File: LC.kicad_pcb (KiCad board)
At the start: 2 copper layers, 60 x 65 mm, 86 parts, among them J1 INPUT+, J10 DISPLAY, J11 ENTER_BUTTON, J12 UP_BUTTON, J2 INPUT-, J3 Barrel_Jack, J4 EXT_CLK, J5 CLKSRC, J6 SIGSRC, J7 EXT_SIG, J8 UNUSED, J9 PROG, Q1 BC817, Q2 BC817, SW1 RESET_BTN, U1 Omron_G2V, U10 74HC590PW,118, U11 74HCS251, U12 AVR32DB28x-xSO, U2 L7805, U3 74AHC1G04, U4 Omron_G2E, U5 74AHC1G14, U6 74AHC1G04, U7 LT1719CS6, U8 74AUC1G74, U9 74AUC2G125, Y1 10MHz

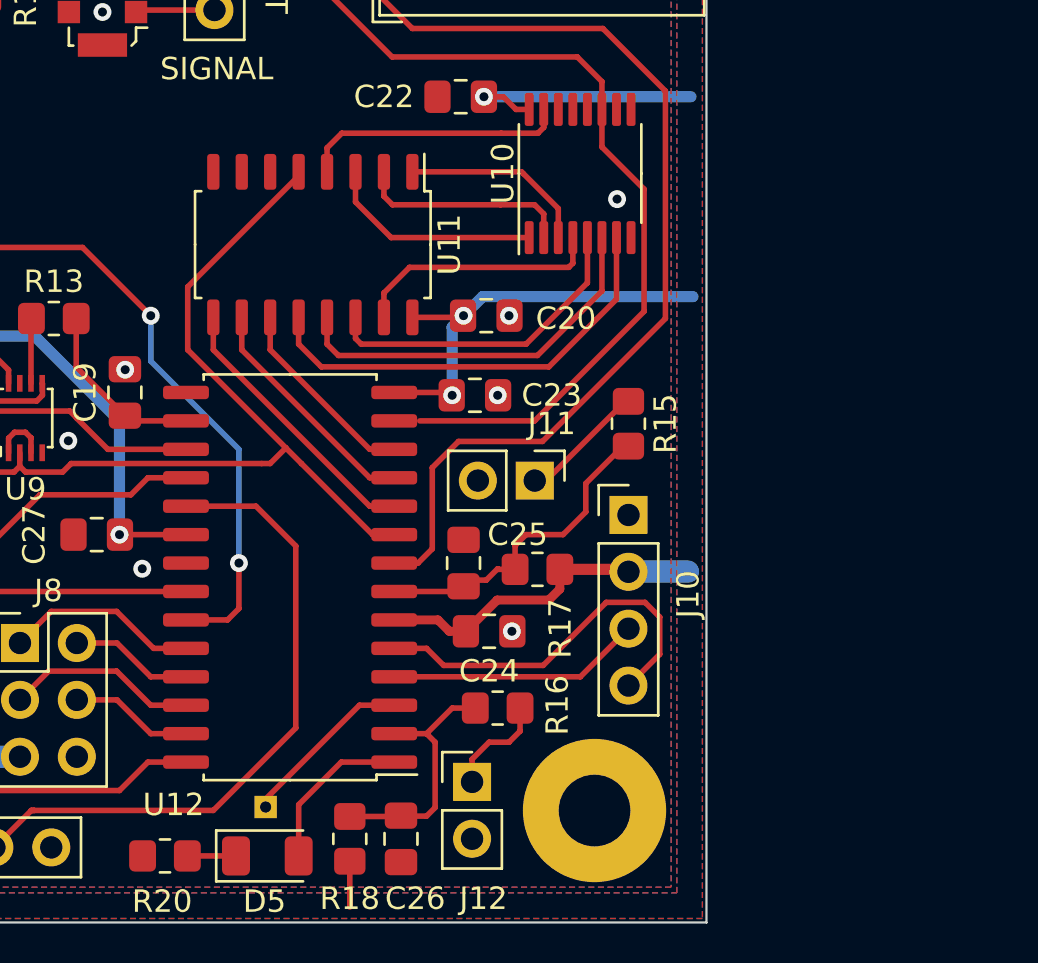
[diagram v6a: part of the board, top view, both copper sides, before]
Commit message: Updated schematic for 5V devices in TIC, PCB is in todo
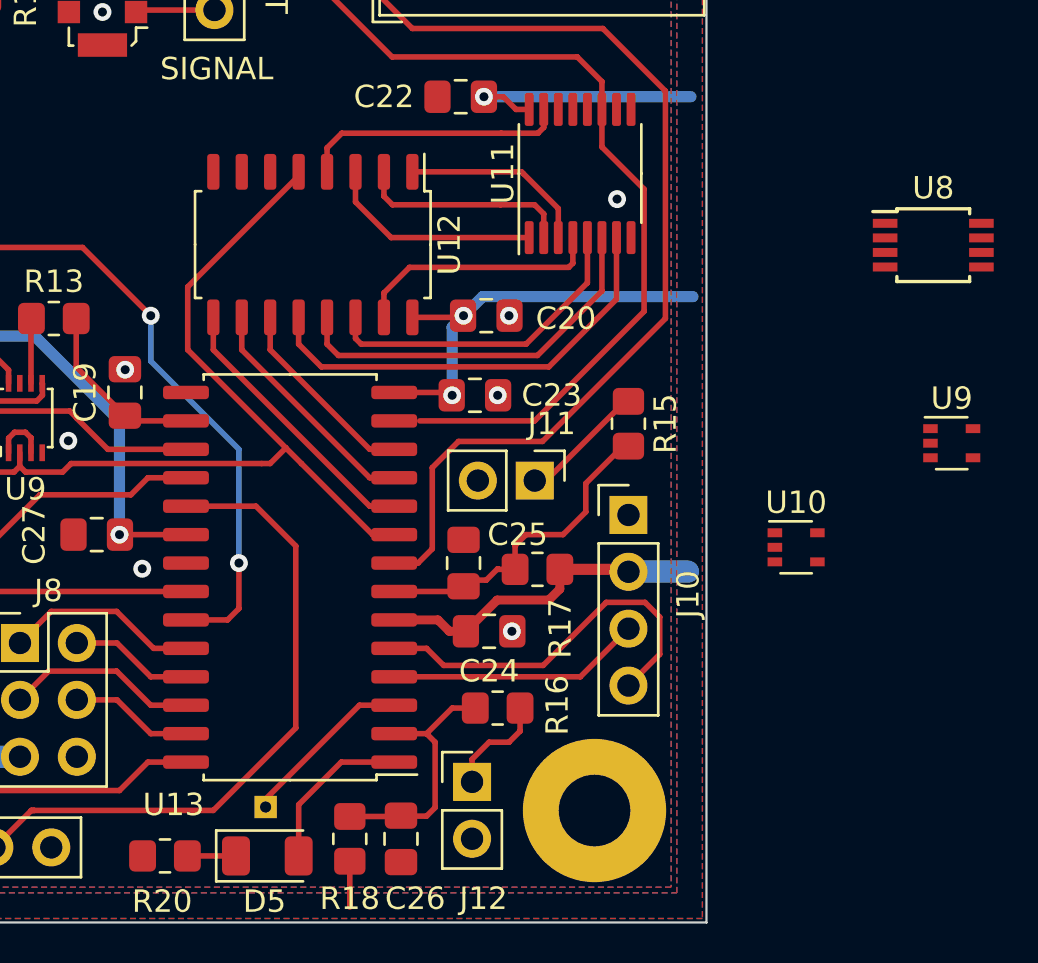
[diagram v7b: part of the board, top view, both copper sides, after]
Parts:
- added U10: 74LVC1G125SE-7, Package_TO_SOT_SMD:SOT-353_SC-70-5, F.Cu at (199.0, 83.2)
- added U8: 74LVC2G74DP,125, Package_SO:TSSOP-8_3x3mm_P0.65mm, F.Cu at (205.1, 69.7)
- added U9: 74LVC1G125SE-7, Package_TO_SOT_SMD:SOT-353_SC-70-5, F.Cu at (206.0, 78.6)
- C19: value 470p -> 680p
- R13: value 200R -> 150R
- renumbered U10 to U11, U11 to U12, U12 to U13

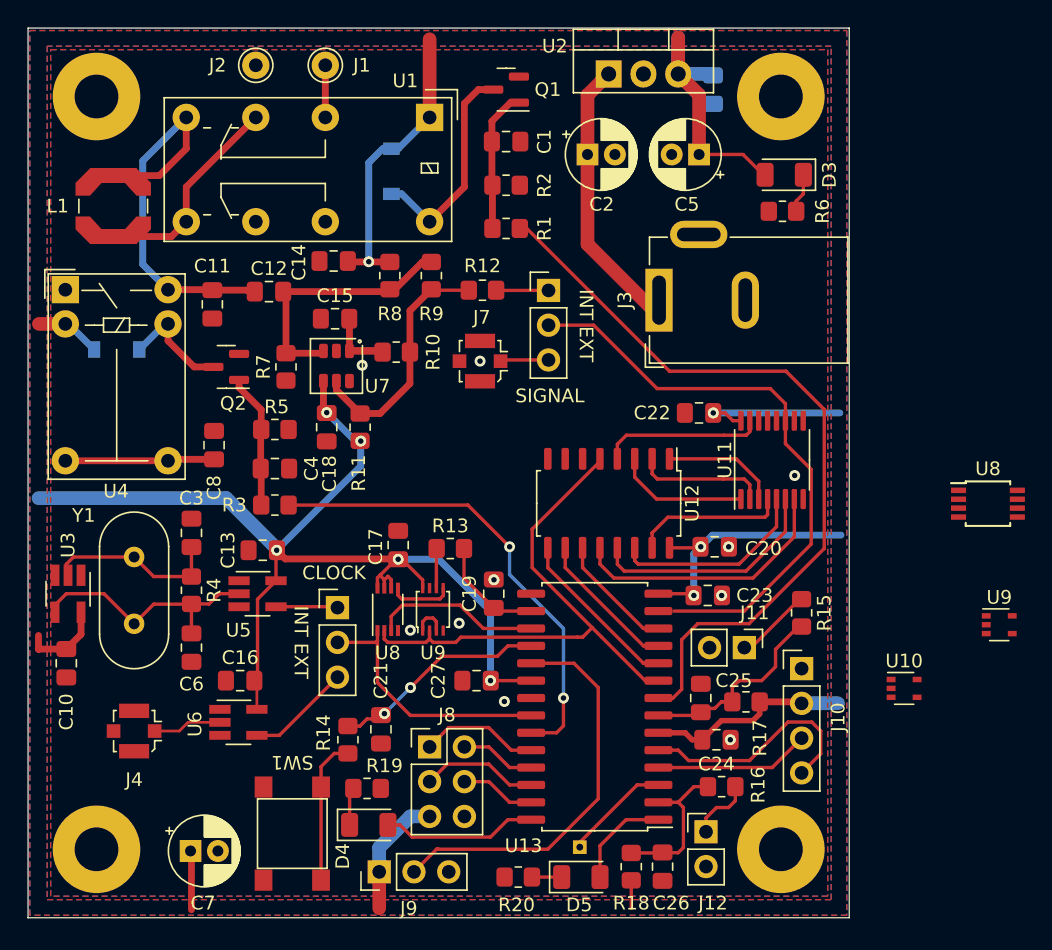
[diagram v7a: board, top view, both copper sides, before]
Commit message: Updated schematic with correct 5V devices
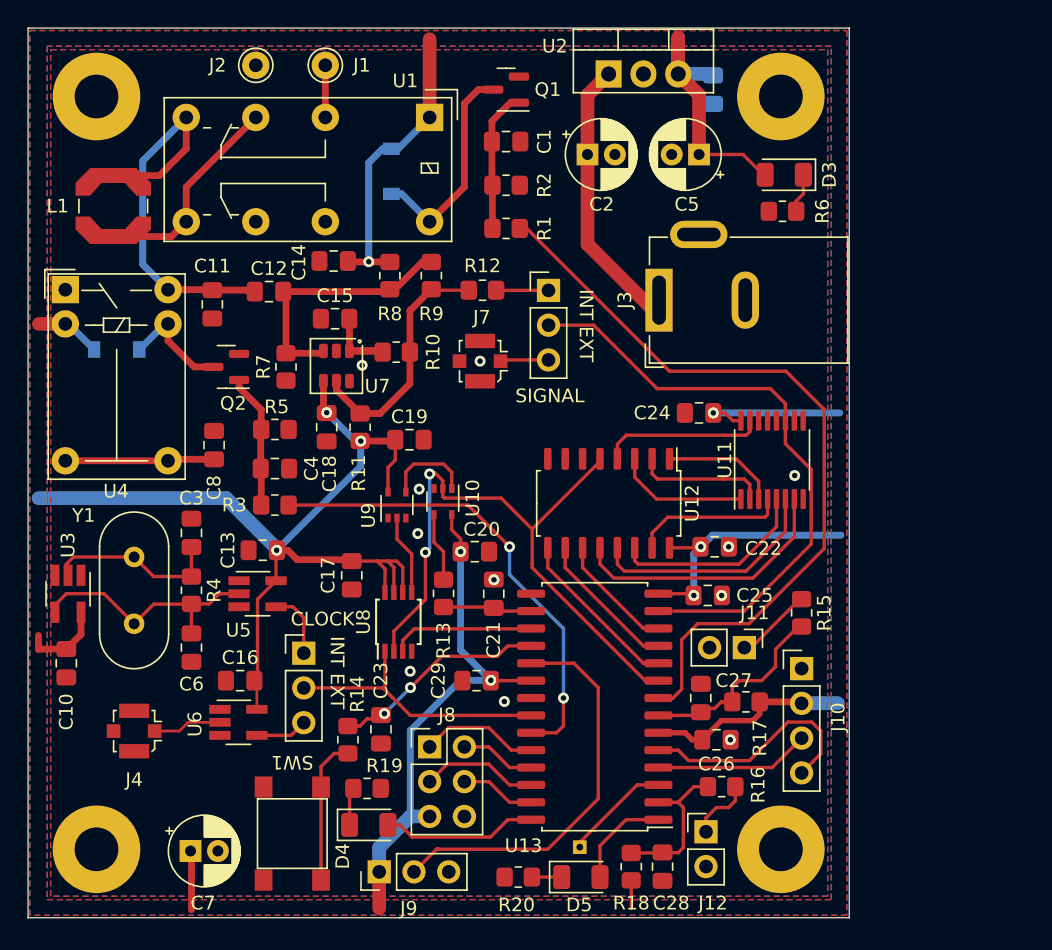
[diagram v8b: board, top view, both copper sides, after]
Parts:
- removed the U8 at (161.3, 77.5)
- removed the U9 at (164.6, 77.5)
- added C19: 100n, Capacitor_SMD:C_0805_2012Metric_Pad1.18x1.45mm_HandSolder, F.Cu at (162.9, 65.1)
- added C20: 100n, Capacitor_SMD:C_0805_2012Metric_Pad1.18x1.45mm_HandSolder, F.Cu at (167.6, 73.3)
- moved U9 44.9 mm to (162.0, 69.8), turned to 90 degrees
- moved U8 43.9 mm to (162.1, 78.4), turned to 90 degrees
- moved U10 36.4 mm to (165.3, 69.6), turned to -90 degrees
- moved J5 4.14 mm to (155.1, 80.7)
- moved C17 4.05 mm to (158.6, 75.0), turned to 90 degrees
- moved R13 3.31 mm to (165.4, 76.3), turned to 90 degrees
- renumbered C19 to C21, C20 to C22, C21 to C23, C22 to C24, C23 to C25, C24 to C26, C25 to C27, C26 to C28, C27 to C29
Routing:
- net +5V: track 194.8 -> 214.2 mm
- net /SIG_RED: track 39.8 -> 46.6 mm, vias 0 -> 2
- net Net-(U10-Pad1): track 0.00 -> 6.51 mm
- net Net-(J5-Pad3): track 7.65 -> 3.81 mm
- net Net-(U9-Pad1): track 2.53 -> 0.00 mm
- net Net-(R13-Pad2): track 2.90 -> 5.05 mm
- net /ICP1: track 12.3 -> 10.5 mm
- net /IPOL: track 8.06 -> 6.52 mm
- net Net-(U8-Pad5): track 4.59 -> 5.88 mm
- net /AVRCLK: track 19.0 -> 20.2 mm
- net GND: vias 10 -> 11
